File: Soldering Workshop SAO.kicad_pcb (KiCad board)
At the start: 2 copper layers, 39.4 x 40.4 mm, 19 parts, among them J1 Conn_02x03_Odd_Even, SW1 SW_SPDT, U1 LMC555xM

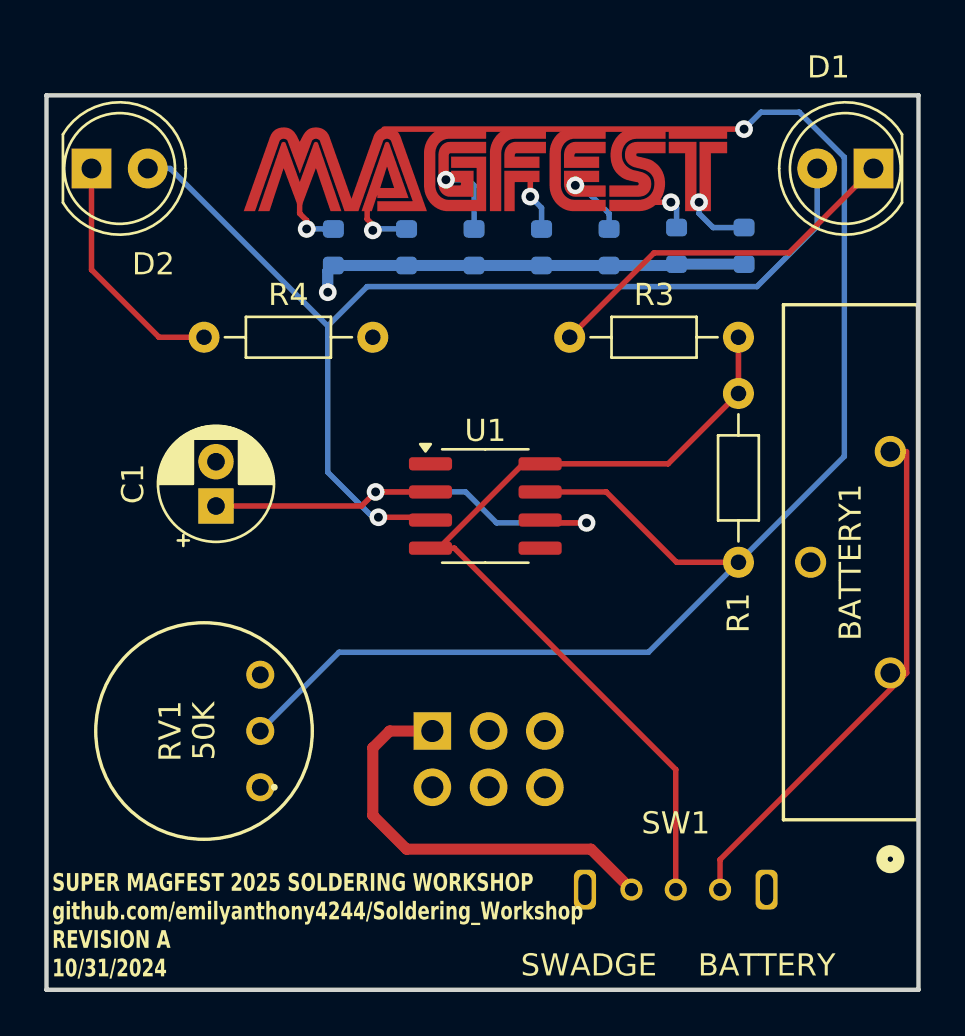
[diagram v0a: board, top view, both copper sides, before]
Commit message: Revision B
do not blindly trust schematics you find on the internet

Connect Th to Tr
Disconnect RV1 from GND
Connect RV1 to Th
Flip D1
Put D1 on silk
put MAGFEST on the schematic
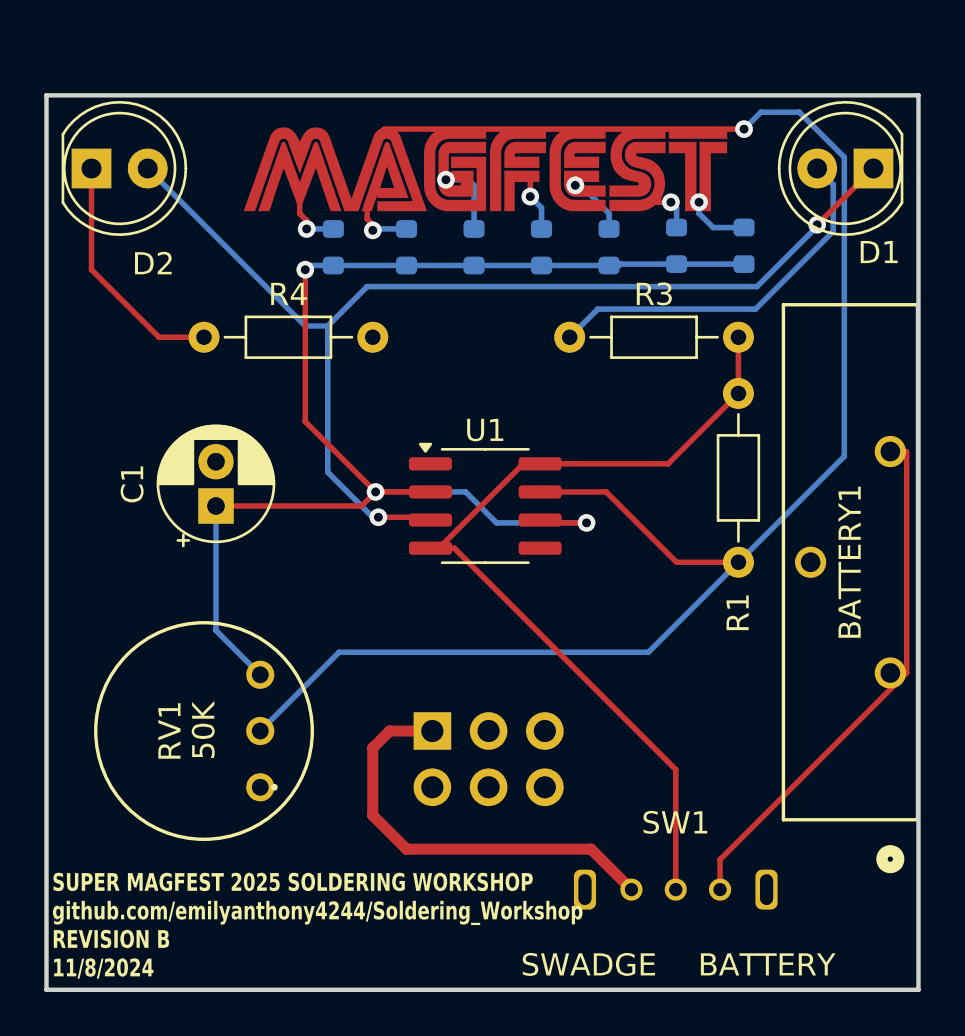
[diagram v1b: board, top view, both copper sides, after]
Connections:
- A pad 2: GND -> Net-(U1-THR)
- D2 pad 2: Net-(D1-A) -> Net-(D1-K)
- E pad 2: GND -> Net-(U1-THR)
- F pad 2: GND -> Net-(U1-THR)
- G pad 2: GND -> Net-(U1-THR)
- M pad 2: GND -> Net-(U1-THR)
- R3 pad 1: Net-(D1-K) -> Net-(D1-A)
- RV1 pad 3: GND -> Net-(U1-THR)
- S pad 2: GND -> Net-(U1-THR)
- T pad 2: GND -> Net-(U1-THR)
- U1 pad 3: Net-(D1-A) -> Net-(D1-K)
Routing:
- net Net-(U1-THR): track 23.0 -> 62.7 mm, vias 2 -> 3
- net Net-(D1-K): track 17.1 -> 51.0 mm, vias 0 -> 2
- net Net-(D1-A): track 49.8 -> 17.0 mm, vias 1 -> 0
- net GND: track 19.9 -> 0.00 mm, vias 1 -> 0
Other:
- board text added: "SUPER MAGFEST 2025 SOLDERING WORKSHOP github.com/emilyanthony4244/Soldering_Workshop REVISION B 11/8/2024"
- board text removed: "SUPER MAGFEST 2025 SOLDERING WORKSHOP github.com/emilyanthony4244/Soldering_Workshop REVISION A 10/31/2024"
